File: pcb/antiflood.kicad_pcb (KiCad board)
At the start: 2 copper layers, 88 x 84 mm, 89 parts, among them J1 Barrel_Jack, J10 Screw_Terminal_01x02, J11 Screw_Terminal_01x02, J12 Screw_Terminal_01x02, J13 Screw_Terminal_01x02, J2 01x03, J3 01x03, J4 Conn_02x05_Odd_Even, J5 Conn_02x04_Odd_Even, J6 Conn_02x05_Odd_Even, J7 Conn_02x03_Odd_Even, J8 Screw_Terminal_01x02, J9 Screw_Terminal_01x02, K1 P-5, K2 P-5, Q1 2N3904, Q2 2N3904, SW1 SW_Push, SW2 SW_Push, SW3 SW_Push, U1 LM1117-3.3, U2 ATMEGA328P-AU, U3 LM7805_TO220, U4 MC34063, U5 MC34063, U6 TP4056, Y1 16MHz

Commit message: Update: scheme, netlist, pcb
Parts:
- removed REF** (x4): MountingHole_3.2mm_M3, Mounting_Holes:MountingHole_3.2mm_M3
- added C13: 0.1, Capacitors_SMD:C_1206, F.Cu at (123.6, 146.7)
- added C14: 22p, Capacitors_SMD:C_1206, F.Cu at (123.6, 154.4)
- added C15: 22p, Capacitors_SMD:C_1206, F.Cu at (117.5, 149.5)
- added D13: LED, LEDs:LED_1206, F.Cu at (123.6, 149.5)
- added D14: LED, LEDs:LED_1206, F.Cu at (123.6, 151.8)
- added R33: 1k, Resistors_SMD:R_0805, F.Cu at (123.1, 142.7)
- added R34: 1k, Resistors_SMD:R_0805, F.Cu at (119.5, 142.7)
- added R35: 1k, Resistors_SMD:R_0805, F.Cu at (115.7, 142.7)
- added R36: 1M, Resistors_SMD:R_0805, F.Cu at (111.9, 142.7)
- C10: value 0.1 -> 22
- C11: value 22p -> 470p
- C12: value 22p -> 100; footprint Capacitors_SMD:C_1206 -> Capacitors_SMD:CP_Elec_6.3x5.7
- C7: value 470p -> 0.1
- C8: value 1n5 -> 0.1
- C9: value 100 -> 22; footprint Capacitors_SMD:CP_Elec_6.3x5.7 -> Capacitors_SMD:C_1206
- D2, D5: value D -> LED; footprint Diodes_SMD:D_SMA -> LEDs:LED_1206
- D3, D8: value LED -> D; footprint LEDs:LED_1206 -> Diodes_SMD:D_SMA
- D6: value D -> YJ SS14
- D7: value LED -> YJ SS14; footprint LEDs:LED_1206 -> Diodes_SMD:D_SMA
- J2: value 01x03 -> Conn_01x03_Male; footprint Connectors_Terminal_Blocks:TerminalBlock_bornier-3_P5.08mm -> Pin_Headers:Pin_Header_Straight_1x03_Pitch2.54mm
- J4: value Conn_02x05_Odd_Even -> 01x03; footprint Socket_Strips:Socket_Strip_Straight_2x05_Pitch2.54mm -> Connectors_Terminal_Blocks:TerminalBlock_bornier-3_P5.08mm
- L1: value 170 -> 220
- R10, R9: value 1k2 -> 10k
- R11: value 180 -> 0.5; footprint Resistors_SMD:R_0805 -> Resistors_SMD:R_2010
- R12: value 3k6 -> 1k
- R13: value 3k6 -> 0.5; footprint Resistors_SMD:R_0805 -> Resistors_SMD:R_2010
- R14: value 0.5 -> 1k; footprint Resistors_SMD:R_2010 -> Resistors_SMD:R_0805
- R15: value 0.5 -> 0.33; footprint Resistors_SMD:R_2010 -> Resistors_SMD:R_0805
- R16: value R -> 1k2
- R17: value 10k -> 1k05
- R18: value R -> 20k
- R19: value 1k5 -> 3k6
- R20, R21: value 3k3 -> 10k
- R23: value 3k3 -> 19k
- R26: value 1k -> 1k5
- R27, R28, R29: value 1k -> 3k3
- R3: value 1k5 -> 2k
- R32: value 1M -> 1k
- R4: value 82 -> 12k
- R5: value 1k -> 10k
- R6: value 0.22 -> 1k
- R7: value 0.33 -> 1k5
- R8: value 1k -> 82
- U1: value LM1117-3.3 -> ATMEGA328P-AU; footprint TO_SOT_Packages_SMD:SOT-223-3_TabPin2 -> Housings_QFP:TQFP-32_7x7mm_Pitch0.8mm
- U2: value ATMEGA328P-AU -> TL7705; footprint Housings_QFP:TQFP-32_7x7mm_Pitch0.8mm -> SMD_Packages:SOIC-8-N
- U3: value LM7805_TO220 -> LM1117-3.3; footprint TO_SOT_Packages_THT:TO-220-3_Horizontal -> TO_SOT_Packages_SMD:SOT-223-3_TabPin2
- U4: value MC34063 -> MT3608; footprint SMD_Packages:SOIC-8-N -> SMD_Packages:Ceramic_Filter
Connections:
- C10 pad 1: /RST -> +12V
- C11 pad 1: /O1 -> Net-(C11-Pad1)
- C12 pad 1: /O2 -> /BAT
- C6 pad 1: +3V3 -> Net-(C6-Pad1)
- C7 pad 1: Net-(C7-Pad1) -> +3V3
- D2 pad 1: +5V -> GND
- D3 pad 1: Net-(D3-Pad1) -> +5V
- D5 pad 1: +12V -> Net-(D5-Pad1)
- D6 pad 1: Net-(D6-Pad1) -> +12V
- D6 pad 2: GND -> Net-(D6-Pad2)
- D7 pad 1: GND -> +12V
- D7 pad 2: Net-(D7-Pad2) -> /EVSS
- D8 pad 1: GND -> Net-(D8-Pad1)
- D8 pad 2: Net-(D8-Pad2) -> GND
- J1 pad 1: +12V -> /EVSS
- J2 pad 1: Net-(J2-Pad1) -> GND
- J2 pad 2: /A6 -> /BTMP
- J2 pad 3: Net-(J2-Pad3) -> /BAT
- J4 pad 1: GND -> Net-(J4-Pad1)
- J4 pad 2: GND -> /A6
- J4 pad 3: /BAT -> Net-(J4-Pad3)
- K1 pad 3: Net-(J2-Pad1) -> Net-(J3-Pad1)
- K1 pad 8: Net-(J3-Pad1) -> Net-(J4-Pad1)
- K2 pad 10: Net-(D2-Pad2) -> Net-(D3-Pad2)
- K2 pad 3: Net-(J2-Pad3) -> Net-(J3-Pad3)
- K2 pad 8: Net-(J3-Pad3) -> Net-(J4-Pad3)
- L1 pad 1: Net-(L1-Pad1) -> /BAT
- L1 pad 2: Net-(D5-Pad2) -> Net-(D6-Pad2)
- L2 pad 1: Net-(D6-Pad1) -> Net-(D8-Pad1)
- Q2 pad 3: Net-(D2-Pad2) -> Net-(D3-Pad2)
- R10 pad 1: Net-(R10-Pad1) -> /BSTE
- R11 pad 1: Net-(L1-Pad1) -> /A6
- R11 pad 2: Net-(R11-Pad2) -> GND
- R12 pad 2: Net-(R12-Pad2) -> Net-(D4-Pad2)
- R13 pad 1: +12V -> /A6
- R13 pad 2: Net-(R10-Pad1) -> GND
- R14 pad 1: /A6 -> +5V
- R14 pad 2: GND -> Net-(D5-Pad2)
- R15 pad 1: /A6 -> Net-(R15-Pad1)
- R15 pad 2: GND -> +12V
- R16 pad 1: /BTMP -> Net-(R16-Pad1)
- R16 pad 2: +5V -> GND
- R18 pad 1: /BTMP -> +12V
- R18 pad 2: GND -> Net-(R17-Pad1)
- R19 pad 1: Net-(J5-Pad4) -> +5V
- R19 pad 2: /WCC -> Net-(R16-Pad1)
- R20 pad 1: Net-(J5-Pad4) -> /BTMP
- R20 pad 2: GND -> +5V
- R21 pad 1: Net-(J5-Pad5) -> Net-(R21-Pad1)
- R21 pad 2: +3V3 -> GND
- R22 pad 1: Net-(J5-Pad7) -> Net-(J5-Pad4)
- R22 pad 2: /WTX -> /WCC
- R23 pad 1: Net-(J5-Pad3) -> /BTMP
- R23 pad 2: +3V3 -> GND
- R24 pad 1: +5V -> Net-(J5-Pad4)
- R24 pad 2: /RST -> GND
- R25 pad 1: Net-(J5-Pad7) -> Net-(J5-Pad5)
- R25 pad 2: GND -> +3V3
- R26 pad 1: Net-(D7-Pad2) -> Net-(J5-Pad7)
- R26 pad 2: /L0 -> /WTX
- R27 pad 1: Net-(D8-Pad2) -> Net-(J5-Pad3)
- R27 pad 2: /L1 -> +3V3
- R28 pad 1: Net-(D9-Pad2) -> +5V
- R28 pad 2: /DBG -> /RST
- R29 pad 1: Net-(D10-Pad2) -> Net-(J5-Pad7)
- R29 pad 2: /L3 -> GND
- R3 pad 1: Net-(D2-Pad2) -> /EVSS
- R3 pad 2: /FCL -> Net-(D2-Pad2)
- R30 pad 1: Net-(D11-Pad2) -> Net-(D9-Pad2)
- R30 pad 2: /L4 -> /L0
- R31 pad 1: Net-(D12-Pad2) -> Net-(D10-Pad2)
- R31 pad 2: /L5 -> /L1
- R32 pad 1: /O1 -> Net-(D11-Pad2)
- R32 pad 2: /O2 -> /DBG
- R4 pad 1: Net-(Q2-Pad2) -> /EVSS
- R4 pad 2: /PCL -> /EPWR
- R5 pad 1: +5V -> /EPWR
- R5 pad 2: Net-(D3-Pad2) -> GND
- R6 pad 1: Net-(L1-Pad1) -> /BAT
- R6 pad 2: /BAT -> /A7
- R7 pad 1: Net-(R7-Pad1) -> Net-(D3-Pad2)
- R7 pad 2: +12V -> /FCL
- R8 pad 1: +5V -> Net-(Q2-Pad2)
- R8 pad 2: Net-(D4-Pad2) -> /PCL
- R9 pad 1: Net-(R12-Pad2) -> /BAT
- R9 pad 2: GND -> /CHGE
- SW2 pad 1: Net-(D2-Pad2) -> Net-(D3-Pad2)
- U1 pad 1: GND -> /BSTE
- U1 pad 2: +5V -> /FON
- U1 pad 3: +12V -> GND
- U2 pad 1: /CHG -> Net-(C6-Pad1)
- U2 pad 2: /FON -> /BAT
- U2 pad 3: GND -> Net-(C8-Pad1)
- U2 pad 4: +5V -> GND
- U2 pad 5: GND -> /CHGE
- U2 pad 6: +5V -> /BSTE
- U2 pad 7: /O1 -> /EPWR
- U2 pad 8: /O2 -> /BAT
- U3 pad 1: +5V -> GND
- U3 pad 2: GND -> +3V3
- U3 pad 3: +3V3 -> +5V
- U4 pad 1: Net-(R7-Pad1) -> Net-(D6-Pad2)
- U4 pad 2: Net-(D6-Pad1) -> GND
- U4 pad 3: Net-(C7-Pad1) -> Net-(R17-Pad1)
- U4 pad 4: GND -> /BSTE
- U4 pad 5: Net-(R12-Pad2) -> /BAT
- U4 pad 6: +12V -> (no net)
- U5 pad 1: Net-(D5-Pad2) -> Net-(R15-Pad1)
- U5 pad 2: GND -> Net-(D8-Pad1)
- U5 pad 3: Net-(C8-Pad1) -> Net-(C11-Pad1)
- U5 pad 5: Net-(R10-Pad1) -> Net-(R16-Pad1)
- U5 pad 6: /BAT -> +12V
- U5 pad 7: Net-(L1-Pad1) -> Net-(R15-Pad1)
- U5 pad 8: Net-(R11-Pad2) -> Net-(R15-Pad1)
- U6 pad 2: Net-(R17-Pad1) -> Net-(R21-Pad1)
- U6 pad 6: Net-(D3-Pad1) -> Net-(D4-Pad1)
- U6 pad 7: Net-(D4-Pad1) -> Net-(D5-Pad1)
- U6 pad 8: /CHG -> /CHGE

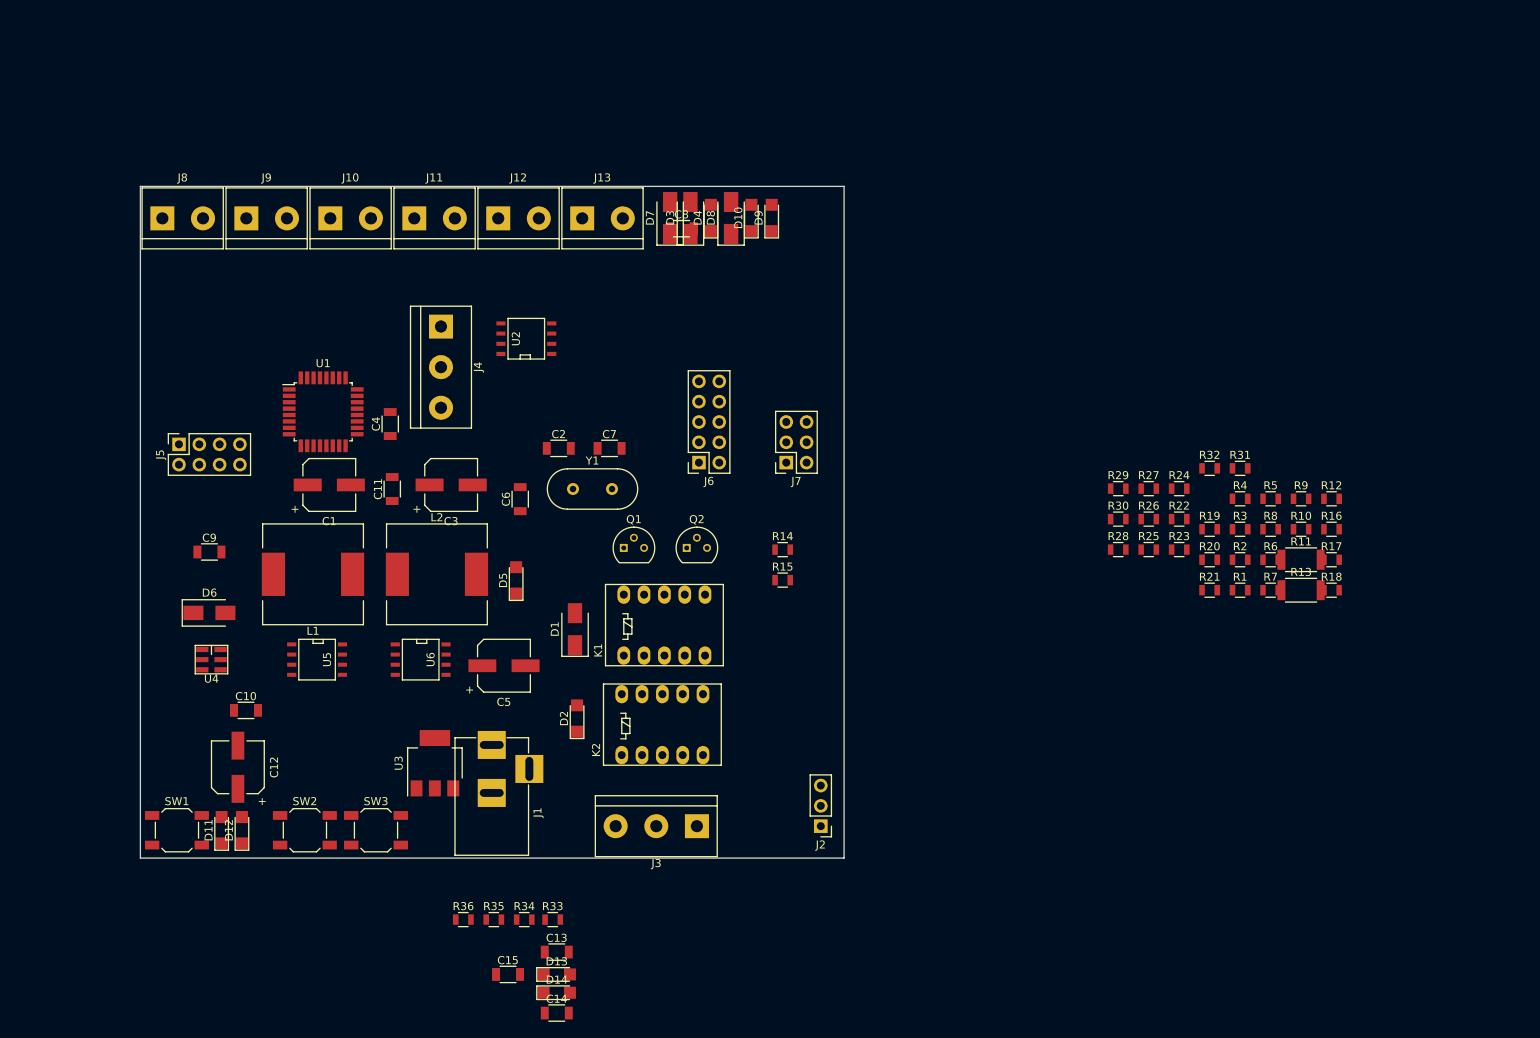
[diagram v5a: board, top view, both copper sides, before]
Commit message: PCB: power units placement
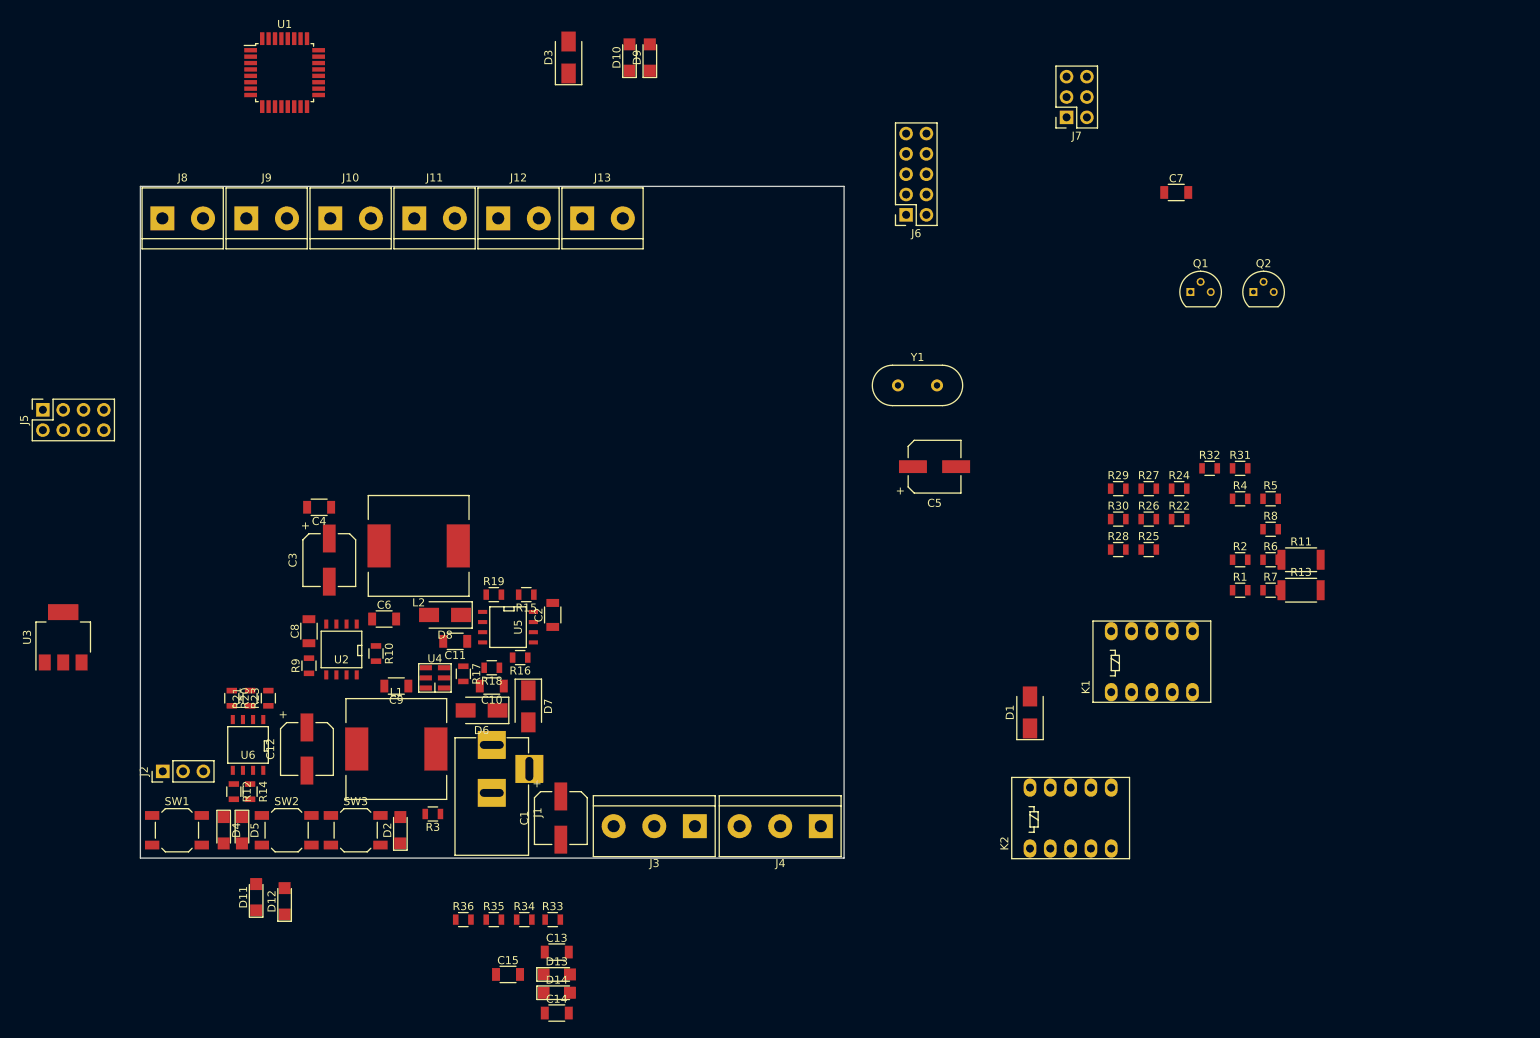
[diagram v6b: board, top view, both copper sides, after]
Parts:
- moved R12 142.1 mm to (83.2, 126.7), turned to 270 degrees
- moved R9 125.8 mm to (92.6, 110.9), turned to 90 degrees
- moved R20 123.5 mm to (82.9, 115.0), turned to 270 degrees
- moved R21 120.8 mm to (85.2, 115.0), turned to 90 degrees
- moved R10 116.7 mm to (101.0, 109.4), turned to 270 degrees
- moved R23 115.4 mm to (87.5, 115.0), turned to 90 degrees
- moved R17 109.5 mm to (111.9, 111.9), turned to 270 degrees
- moved R3 107.0 mm to (108.1, 129.5), turned to 180 degrees
- moved R18 105.5 mm to (115.4, 111.2), turned to 180 degrees
- moved R16 102.7 mm to (119.0, 109.9), turned to 180 degrees
- moved D4 97.8 mm to (81.9, 131.5), turned to 270 degrees
- moved R19 89.9 mm to (115.7, 102.0)
- moved J2 82.6 mm to (74.3, 124.1), turned to 90 degrees
- moved J4 78.5 mm to (156.6, 131.0), turned to 180 degrees
- moved Q1 77.8 mm to (202.8, 64.2)
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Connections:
- D4 pad 2: Net-(D4-Pad2) -> +5V
- D5 pad 2: Net-(D5-Pad2) -> +5V
- R12 pad 1: +5V -> Net-(R12-Pad1)
- R12 pad 2: Net-(D4-Pad2) -> Net-(D4-Pad1)
- R14 pad 1: +5V -> Net-(R14-Pad1)
- R14 pad 2: Net-(D5-Pad2) -> Net-(D5-Pad1)
- U4 pad 6: (no net) -> Net-(U4-Pad6)
- U6 pad 6: Net-(D4-Pad1) -> Net-(R12-Pad1)
- U6 pad 7: Net-(D5-Pad1) -> Net-(R14-Pad1)

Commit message: PCB: all elements on board
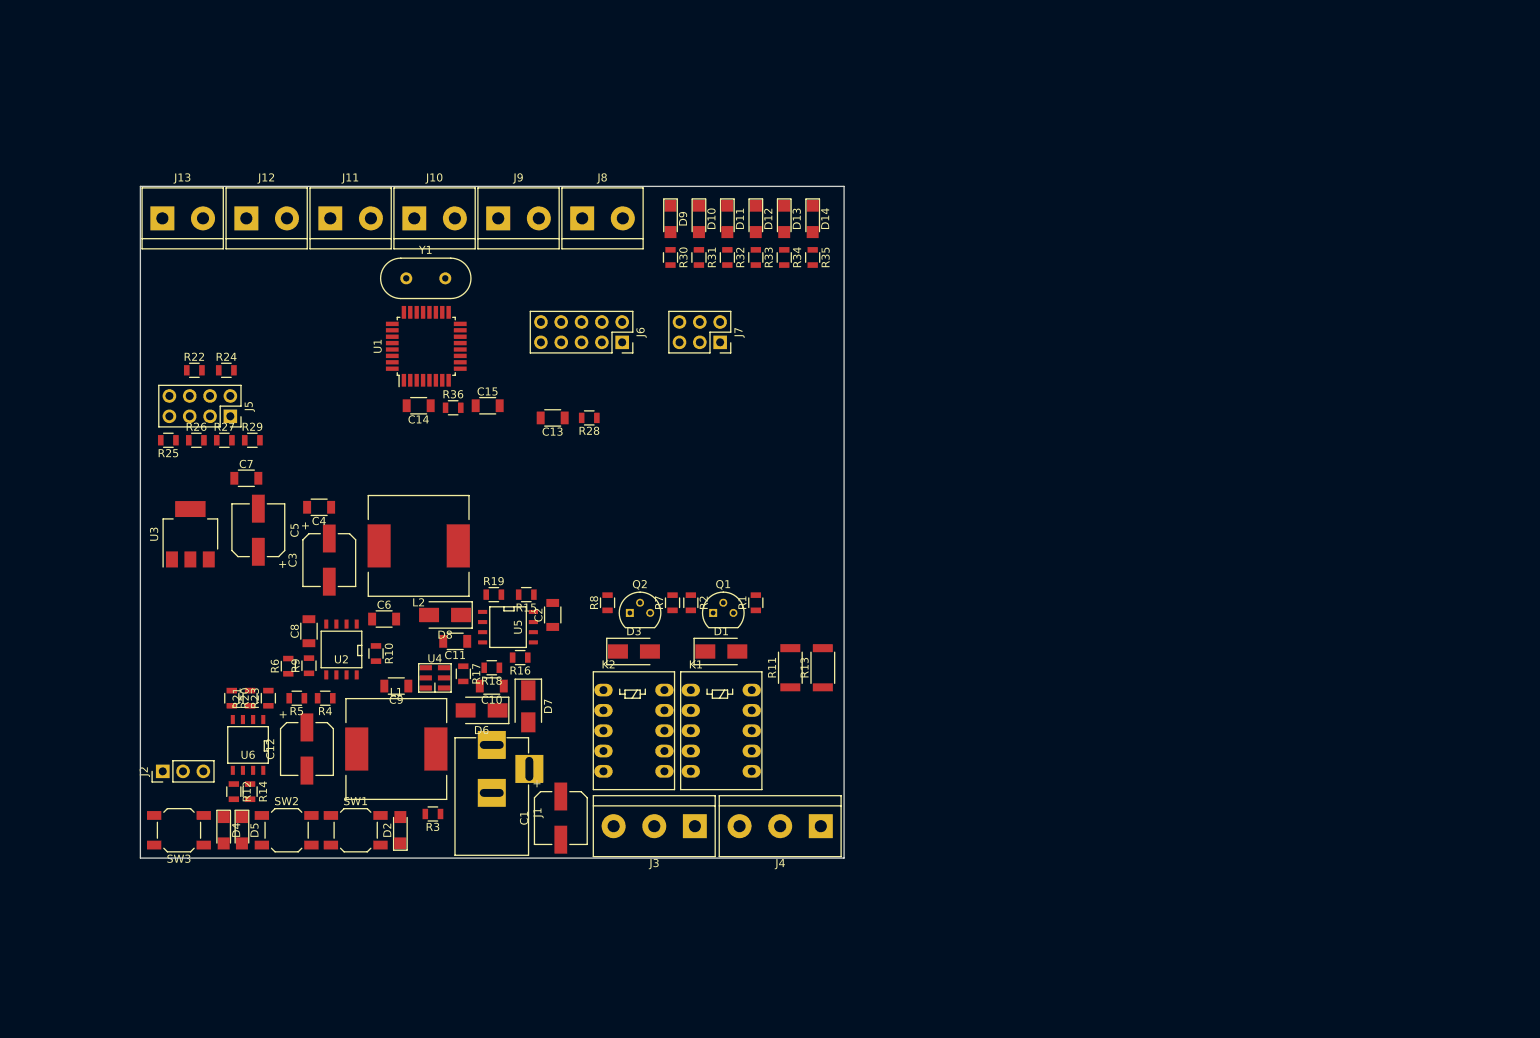
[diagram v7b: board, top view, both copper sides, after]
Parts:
- moved R22 124.6 mm to (78.3, 74.0)
- moved R5 124.3 mm to (91.1, 115.0), turned to 180 degrees
- moved R6 123.6 mm to (90.0, 111.0), turned to 90 degrees
- moved R25 123.4 mm to (75.0, 82.7), turned to 180 degrees
- moved C7 121.7 mm to (84.8, 87.5)
- moved R24 120.1 mm to (82.3, 74.0)
- moved R26 119.5 mm to (78.5, 82.7)
- moved R4 117.1 mm to (94.6, 115.0), turned to 180 degrees
- moved R27 115.8 mm to (82.0, 82.7)
- moved R29 108.5 mm to (85.5, 82.7)
- moved D12 103.7 mm to (148.5, 55.0), turned to 270 degrees
- moved D11 103.3 mm to (144.9, 55.0), turned to 270 degrees
- moved D14 101.9 mm to (155.6, 55.0), turned to 270 degrees
- moved D13 98.7 mm to (152.0, 55.0), turned to 270 degrees
- moved R35 91.9 mm to (155.6, 59.9), turned to 270 degrees
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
